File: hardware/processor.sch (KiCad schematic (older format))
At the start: 23 parts, among them J1 USB_2, P3 CONN_8, P4 CONN_3X2, U10 ATMEGA32U4, U9 USB6B1, X2 16 MHz

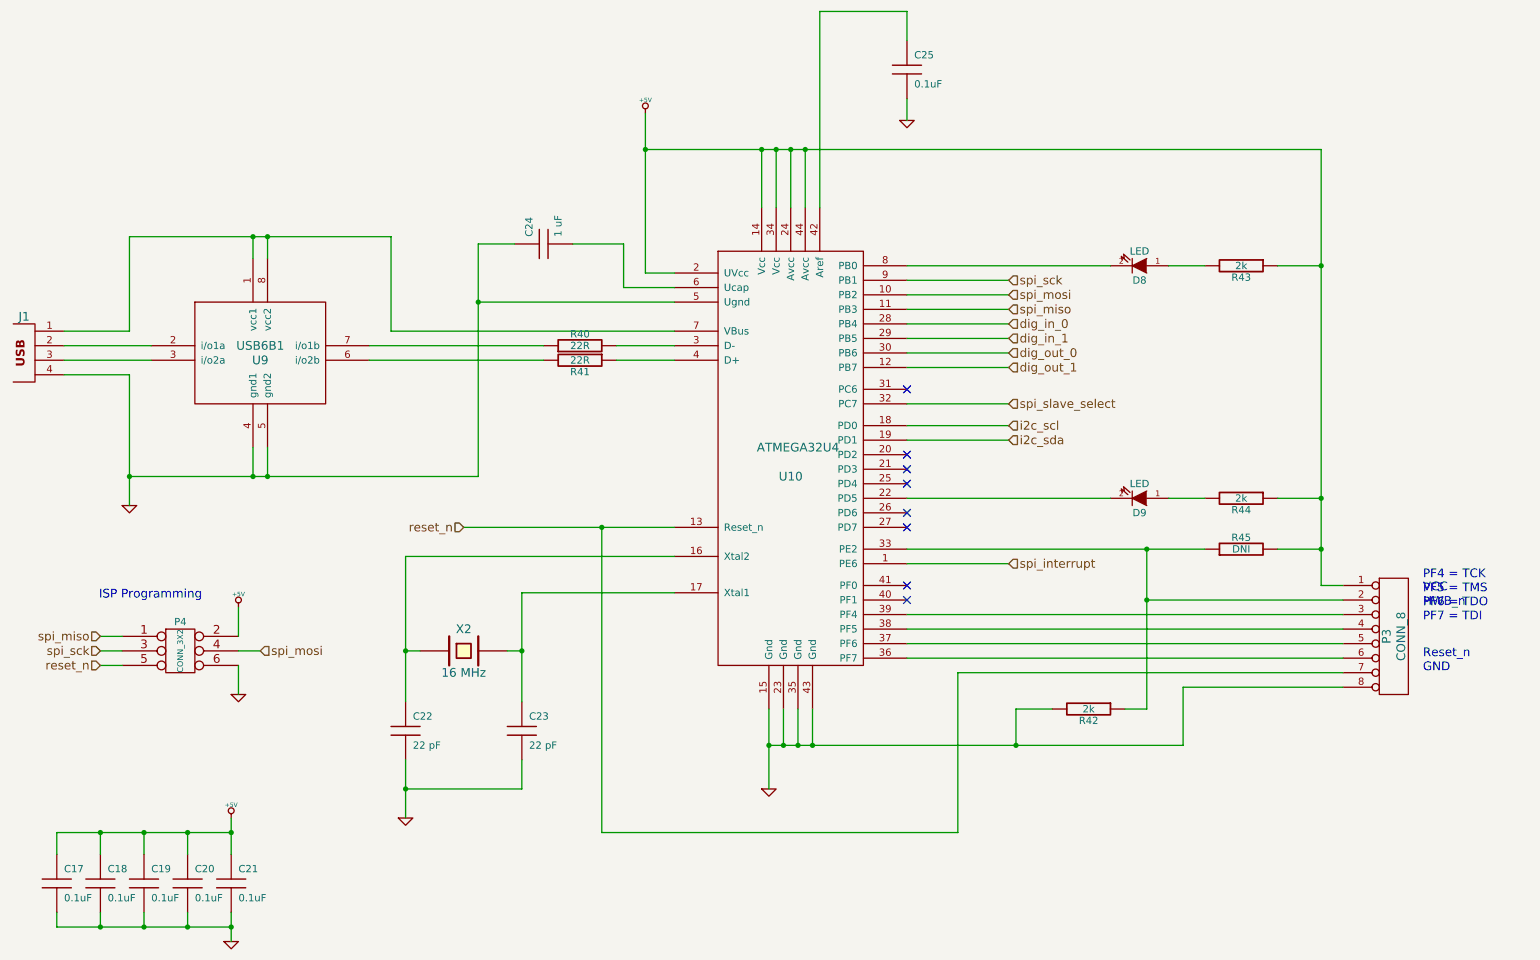
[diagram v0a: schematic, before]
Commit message: changed net labels on spi from off sheet to local
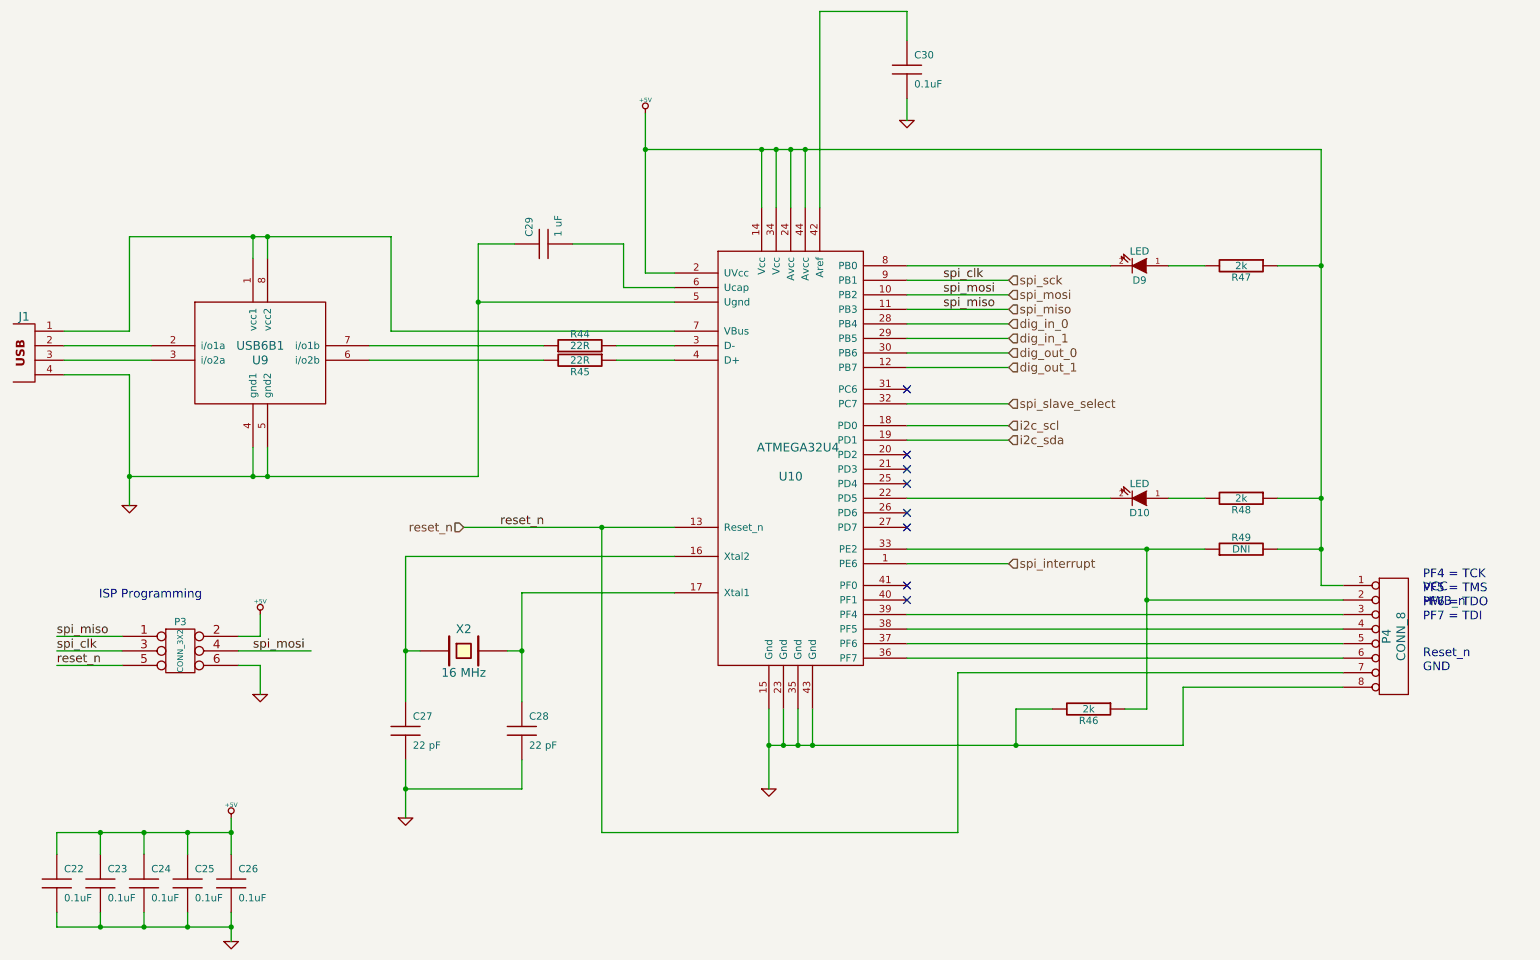
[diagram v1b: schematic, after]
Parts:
- renumbered C17 to C22, C18 to C23, C19 to C24, C20 to C25, C21 to C26, C22 to C27, C23 to C28, C24 to C29, C25 to C30, D9 to D10, D8 to D9, P4 to P3, P3 to P4, R40 to R44, R41 to R45, R42 to R46, R43 to R47, R44 to R48, R45 to R49

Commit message: fixed heirarchy connections for modified sheets
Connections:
- net accel_int_0: now reaches U10.20 (PD2)
- net accel_int_1: now reaches U10.21 (PD3)
- no-connect marks 8 -> 6

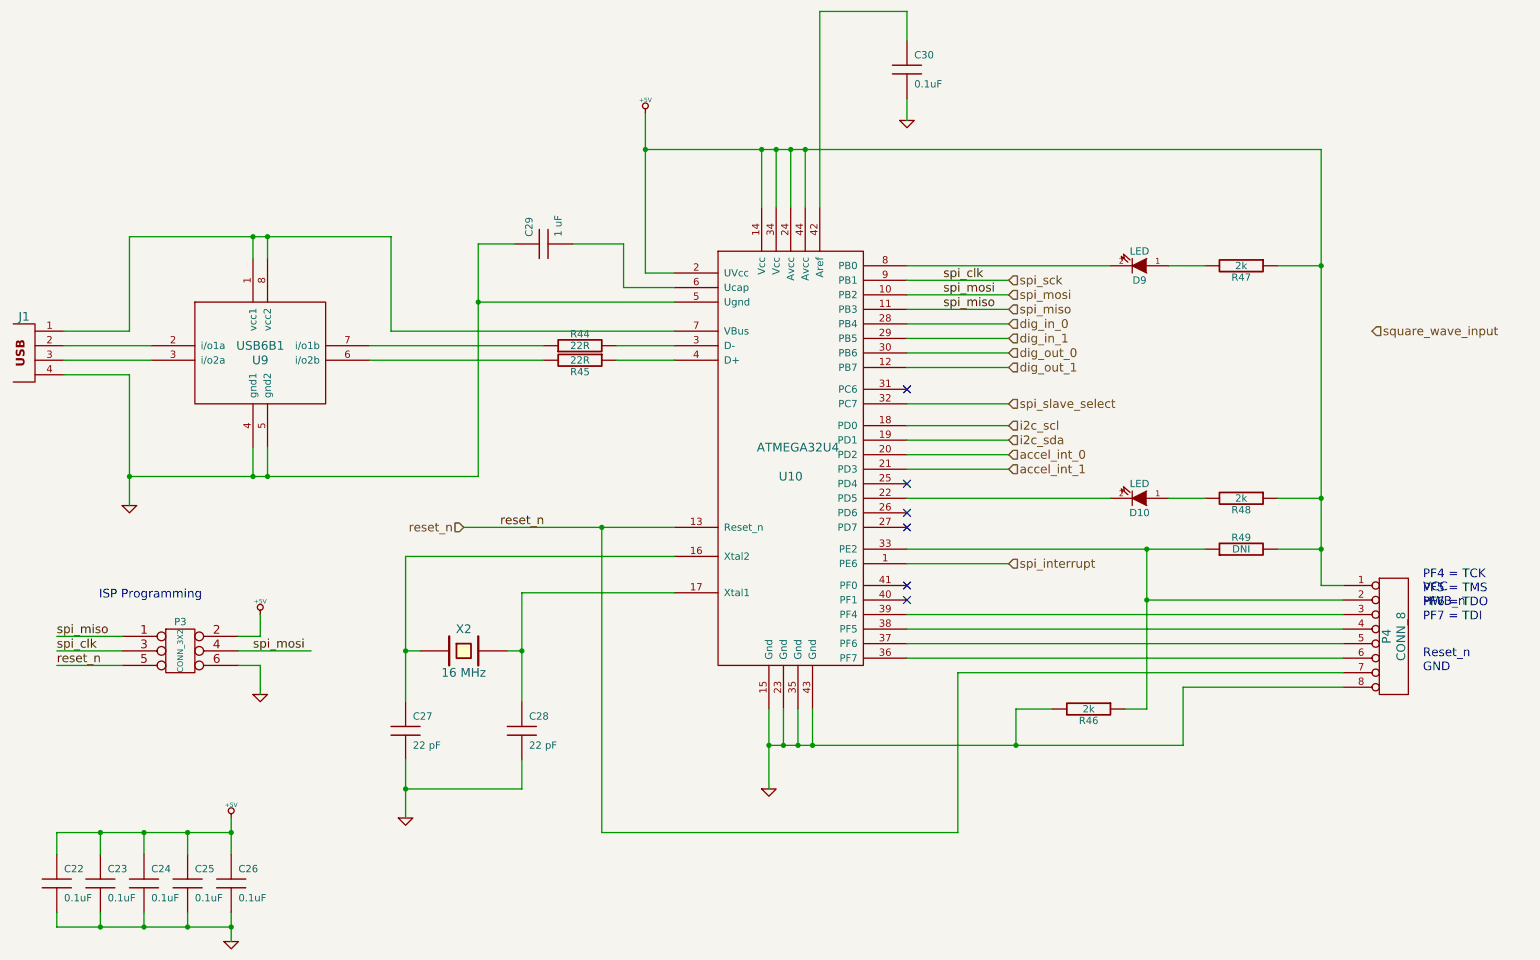
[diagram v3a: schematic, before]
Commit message: removed jtag header and changed the rtc
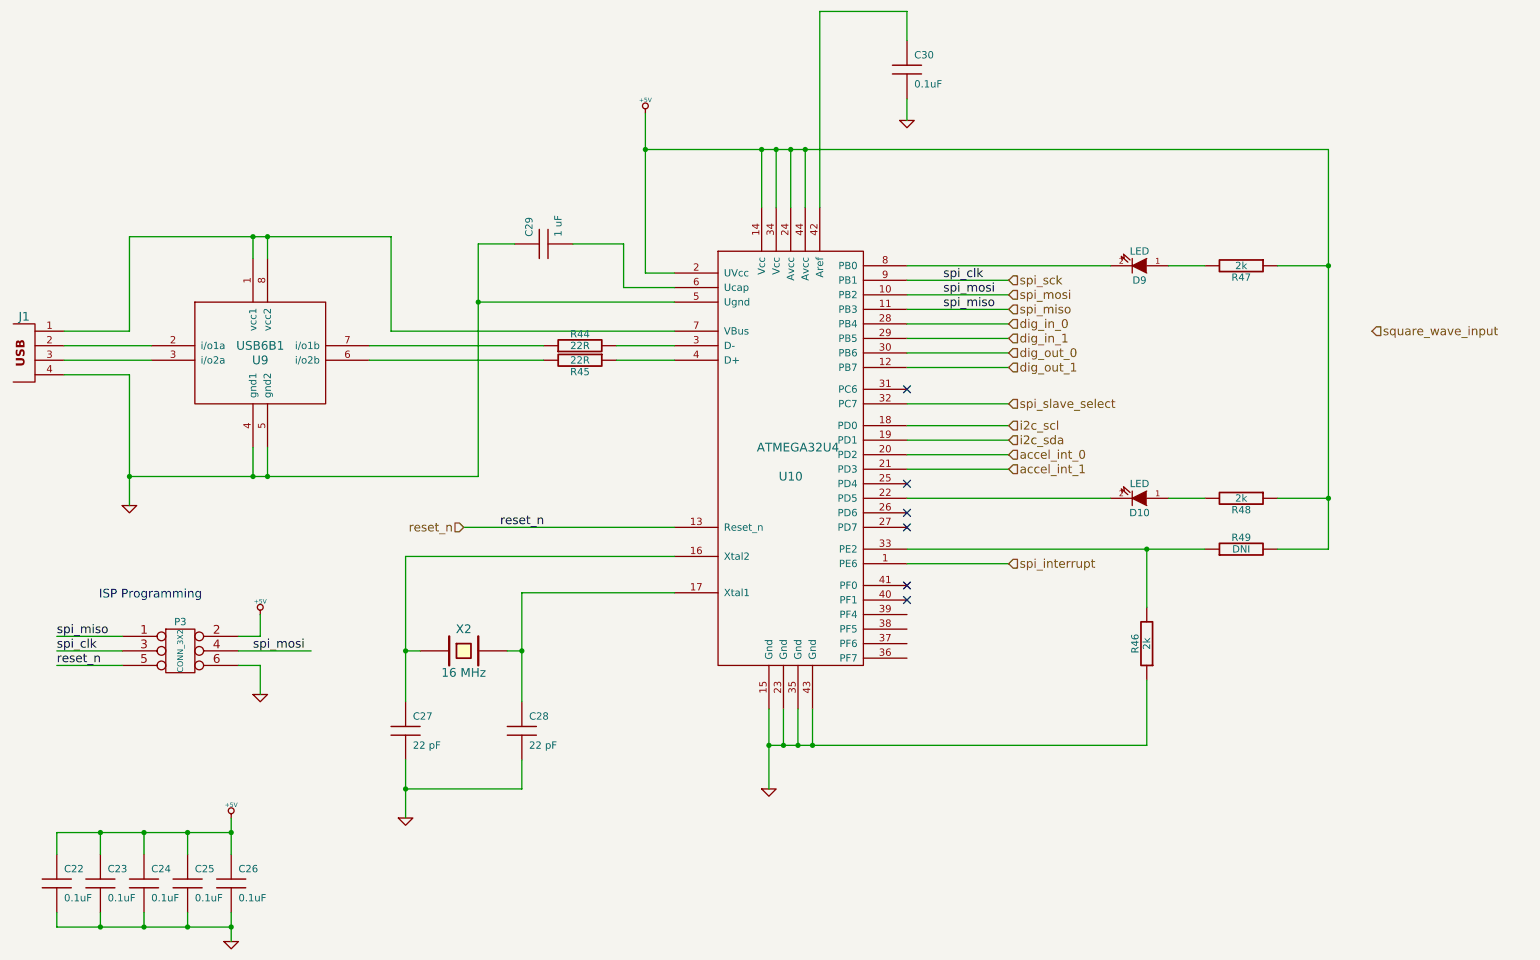
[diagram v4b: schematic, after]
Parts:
- removed P4: CONN_8, symbol CONN_8
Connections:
- net GND: now also R46.1; no longer R46.2
- net at R49.1, U10.33 (PE2): now also R46.2; no longer R46.1
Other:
- note removed: "HWB_n"
- note removed: "PF4 = TCK\nPF5 = TMS\nPF6 = TDO\nPF7 = TDI"
- note removed: "Reset_n\nGND"
- note removed: "VCC\n"
- moved on the sheet: R46
